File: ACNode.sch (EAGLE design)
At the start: 17 parts, among them IC1 74AHC1G04DCK, U2 MAGJACK-POE

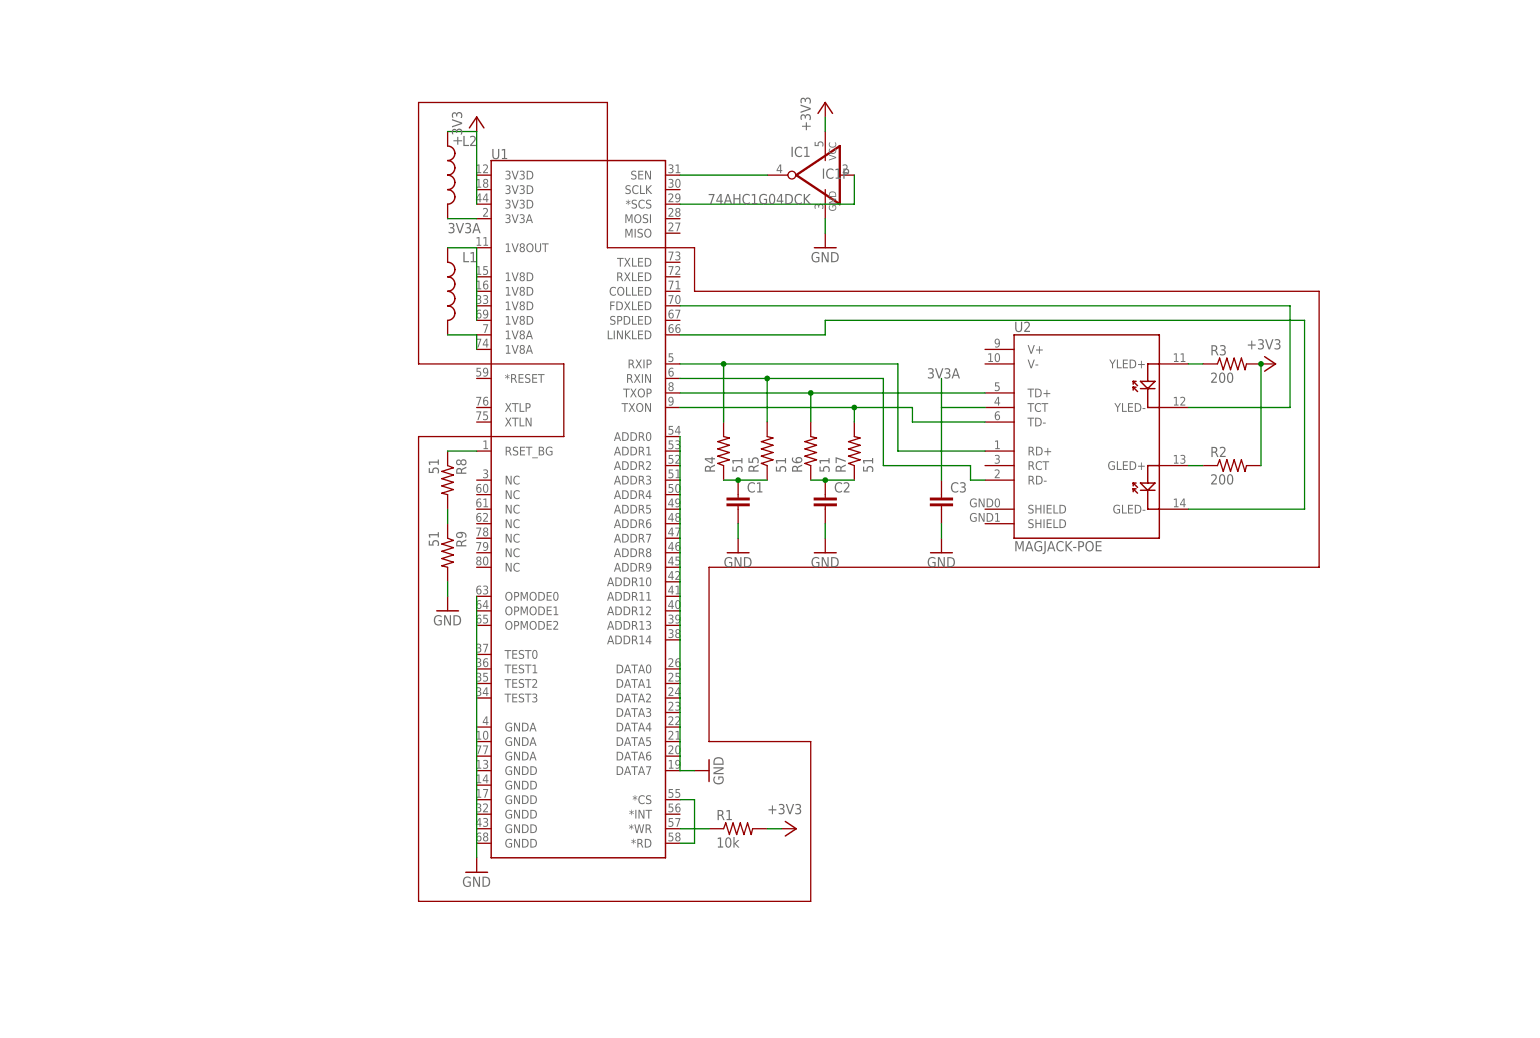
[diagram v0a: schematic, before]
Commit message: Initial wiznet controller design
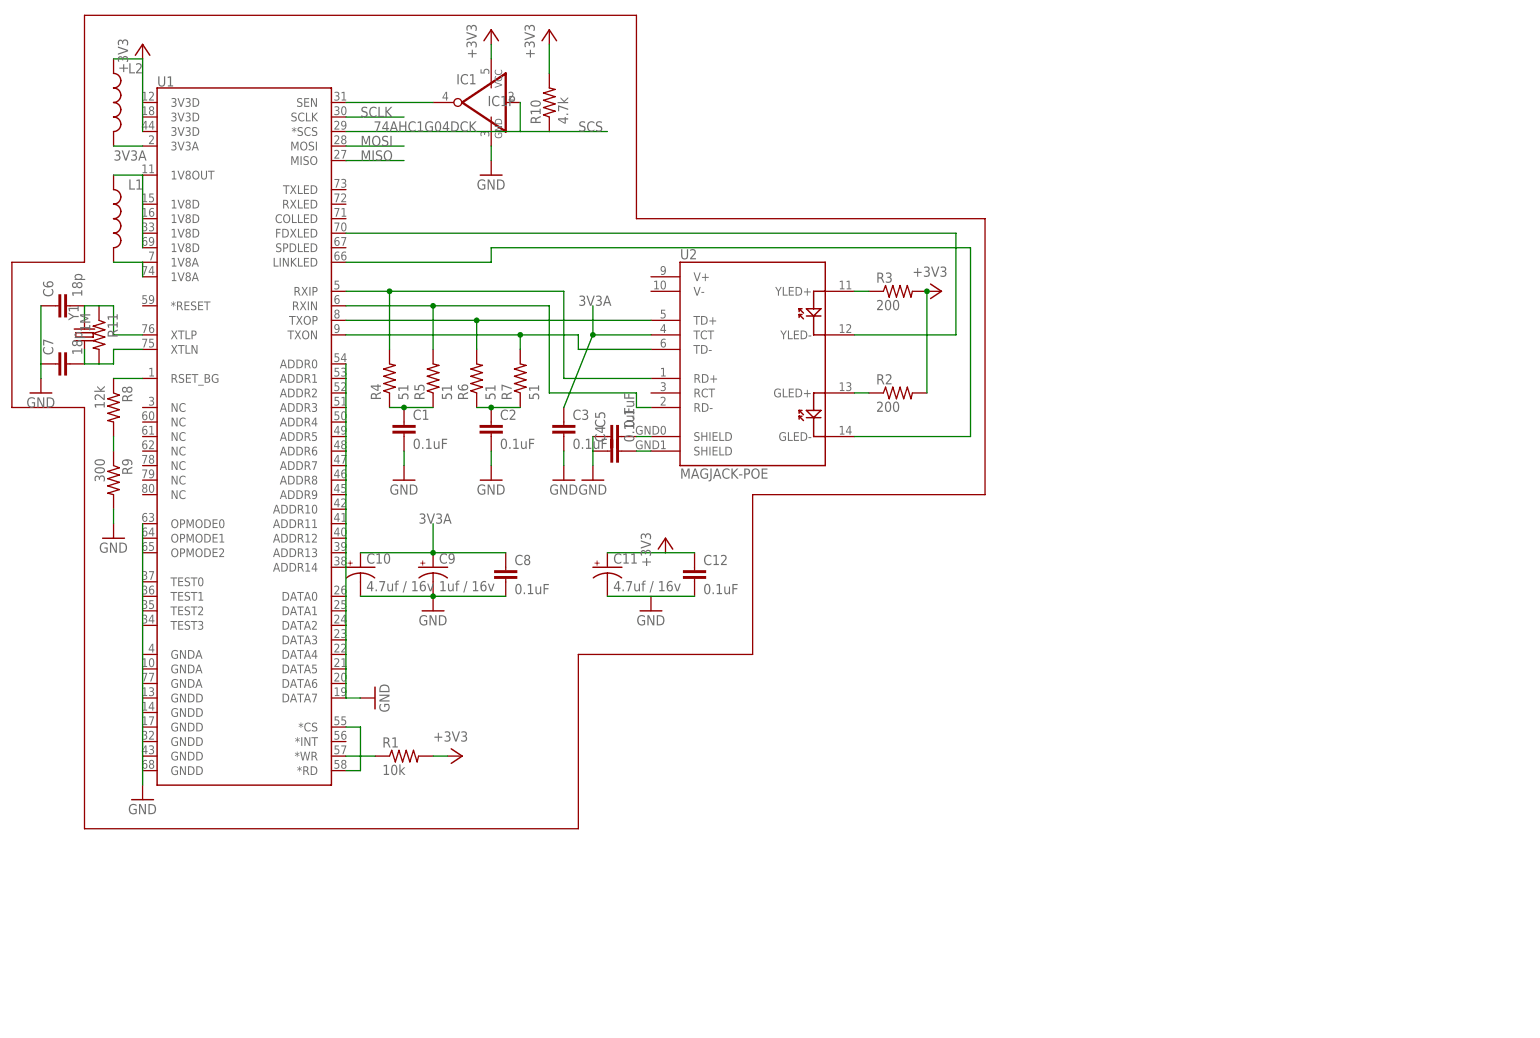
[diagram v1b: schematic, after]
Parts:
- added C10, C11: 4.7uf / 16v, SparkFun-Passives:CAP_POL1206
- added C12, C4, C5, C8: 0.1uF, SparkFun-Passives:CAP0603-CAP
- added C6, C7: 18p, SparkFun-Passives:CAP0603-CAP
- added C9: 1uf / 16v, SparkFun-Passives:CAP_POL1206
- added R10: 4.7k, SparkFun-Passives:RESISTOR0805-RES
- added R11: 1M, SparkFun-Passives:RESISTOR0805-RES
- added Y1: (no value), SparkFun-FreqCtrl:CRYSTALSMD
- C1, C2, C3: value (none) -> 0.1uF
- R8: value 51 -> 12k
- R9: value 51 -> 300
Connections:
- removed net N$2: IC1A.I, U1.*SCS
- new net MISO: U1.MISO
- new net MOSI: U1.MOSI
- new net N$18: C5.2, U2.SHIELD@0
- new net N$19: C4.2, U2.SHIELD@1
- new net N$20: C7.2, R11.2, U1.XTLN, Y1.1
- new net N$21: C6.2, R11.1, U1.XTLP, Y1.2
- new net SCLK: U1.SCLK
- new net SCS: IC1A.I, R10.1, U1.*SCS
- net +3V3: now also C11.+, C12.1, R10.2
- net 3V3A: now also C10.+, C8.1, C9.+
- net GND: now also C10.-, C11.-, C12.2, C4.1, C5.1, C6.1, C7.1, C8.2, C9.-
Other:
- moved on the sheet: C1, C2, C3, IC1, IC1P, L1, L2, R1, R2, R3, R4, R5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

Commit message: Add basic MCU
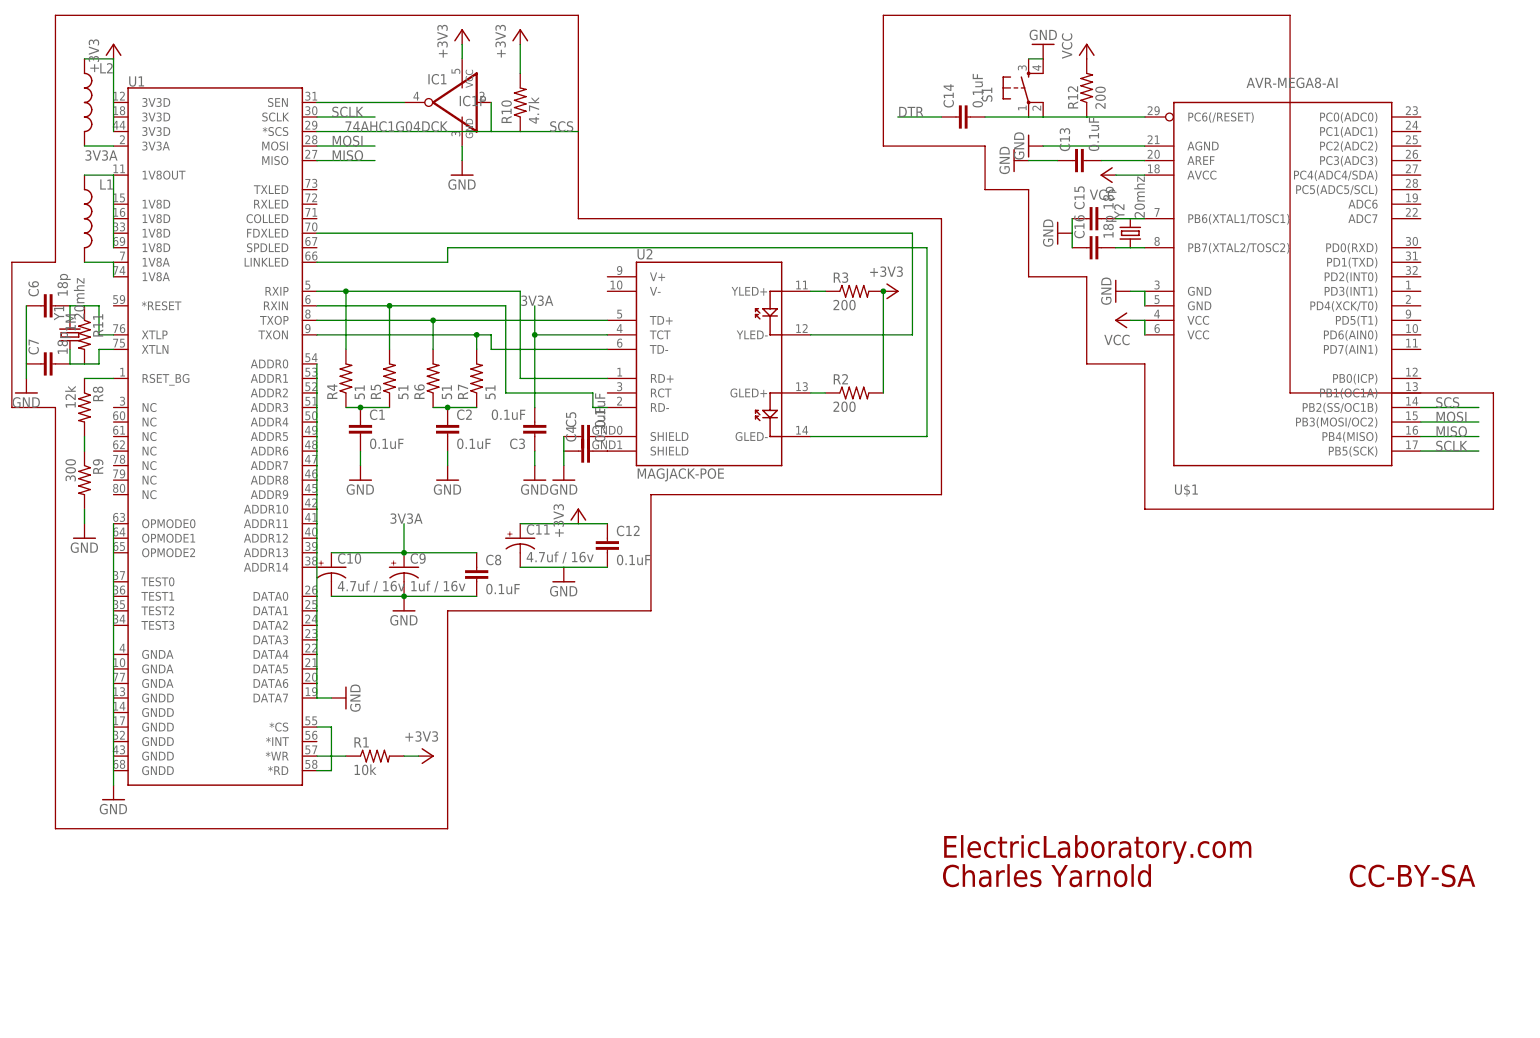
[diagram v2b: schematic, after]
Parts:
- added C13, C14: 0.1uF, SparkFun-Passives:CAP0603-CAP
- added C15, C16: 18p, SparkFun-Passives:CAP0603-CAP
- added R12: 200, SparkFun-Passives:RESISTOR0805-RES
- added S1: (no value), SparkFun-Electromechanical:TAC_SWITCHSMD
- added U$1: AVR-MEGA8-AI, SparkFun-DigitalIC:AVR-MEGA8-AI
- added Y2: 20mhz, SparkFun-FreqCtrl:CRYSTALSMD
- Y1: value (none) -> 20mhz
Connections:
- new net DTR: C14.1
- new net N$2: C13.2, U$1.AREF
- new net N$22: C15.2, U$1.PB6(XTAL1/TOSC1), Y2.2
- new net N$23: C14.2, R12.1, S1.1, S1.2, U$1.PC6(/RESET)
- new net N$24: C16.2, U$1.PB7(XTAL2/TOSC2), Y2.1
- new net VCC: R12.2, U$1.AVCC, U$1.VCC@1, U$1.VCC@2
- net 3V3A: now also C3.2; no longer C3.1
- net GND: now also C13.1, C15.1, C16.1, C3.1, S1.3, S1.4, U$1.AGND, U$1.GND@1, U$1.GND@2; no longer C3.2
- net MISO: now also U$1.PB4(MISO)
- net MOSI: now also U$1.PB3(MOSI/OC2)
- net SCLK: now also U$1.PB5(SCK)
- net SCS: now also U$1.PB2(SS/OC1B)
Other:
- note added: "CC-BY-SA"
- note added: "Charles Yarnold"
- note added: "ElectricLaboratory.com"
- moved on the sheet: C1, C10, C11, C12, C2, C3, C4, C5, C6, C7, C8, C9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

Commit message: Add pullup resistors, FDTI port and resize resistors
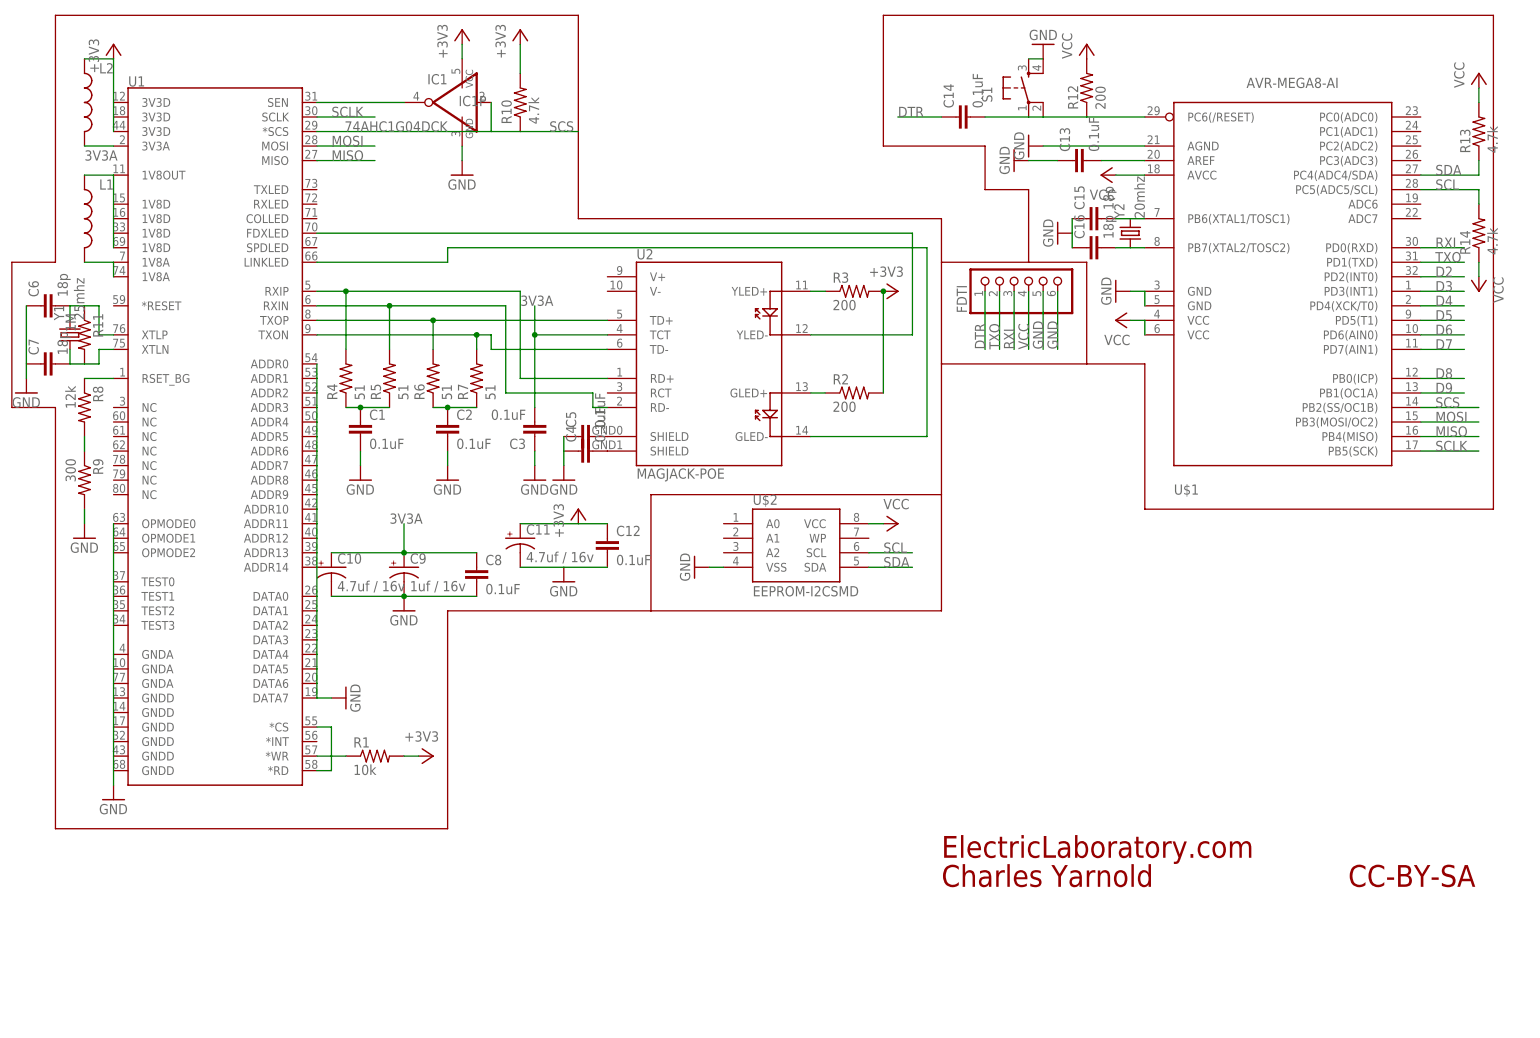
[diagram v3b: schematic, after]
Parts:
- added FDTI: (no value), pinhead:PINHD-1X6
- added R13, R14: 4.7k, SparkFun-Passives:RESISTOR0603-RES
- added U$2: EEPROM-I2CSMD, SparkFun-DigitalIC:EEPROM-I2CSMD
- R1, R10, R12, R2, R3, R8, R9: device SparkFun-Passives:RESISTOR0805-RES -> SparkFun-Passives:RESISTOR0603-RES
- Y1: value 20mhz -> 25mhz
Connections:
- new net D2: U$1.PD2(INT0)
- new net D3: U$1.PD3(INT1)
- new net D4: U$1.PD4(XCK/T0)
- new net D5: U$1.PD5(T1)
- new net D6: U$1.PD6(AIN0)
- new net D7: U$1.PD7(AIN1)
- new net D8: U$1.PB0(ICP)
- new net D9: U$1.PB1(OC1A)
- new net RXI: FDTI.3, U$1.PD0(RXD)
- new net SCL: R14.2, U$1.PC5(ADC5/SCL), U$2.SCL
- new net SDA: R13.1, U$1.PC4(ADC4/SDA), U$2.SDA
- new net TXO: FDTI.2, U$1.PD1(TXD)
- net DTR: now also FDTI.1
- net GND: now also FDTI.5, FDTI.6, U$2.VSS
- net VCC: now also FDTI.4, R13.2, R14.1, U$2.VCC
